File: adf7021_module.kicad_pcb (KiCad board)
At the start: 4 copper layers, 62.5 x 28 mm, 75 parts, among them J1 Conn_Board2Board, J2 Conn_Coaxial, J3 Conn_Coaxial, J4 Conn_goldpin, J5 Conn_Coaxial, J6 Conn_Coaxial, J7 RFShield_OnePiece, U1 ADF7021, X1 19.68MHz

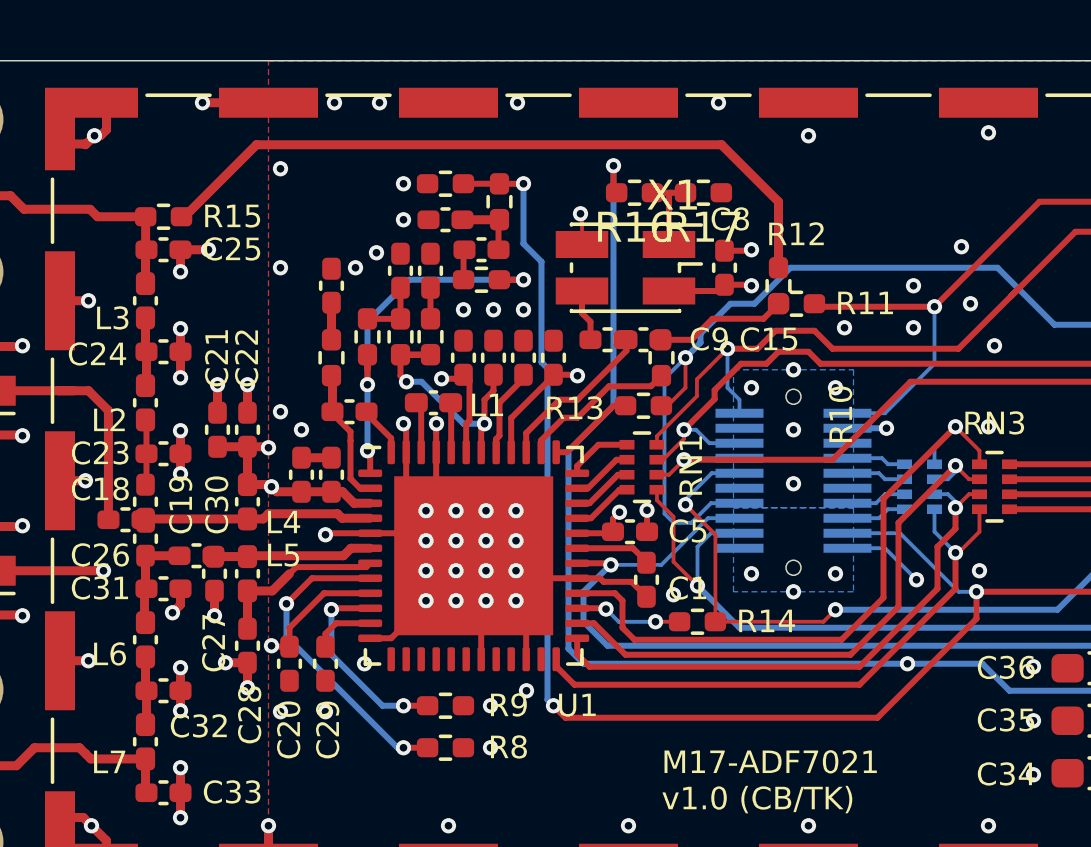
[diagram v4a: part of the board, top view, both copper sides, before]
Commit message: adding fab outputs
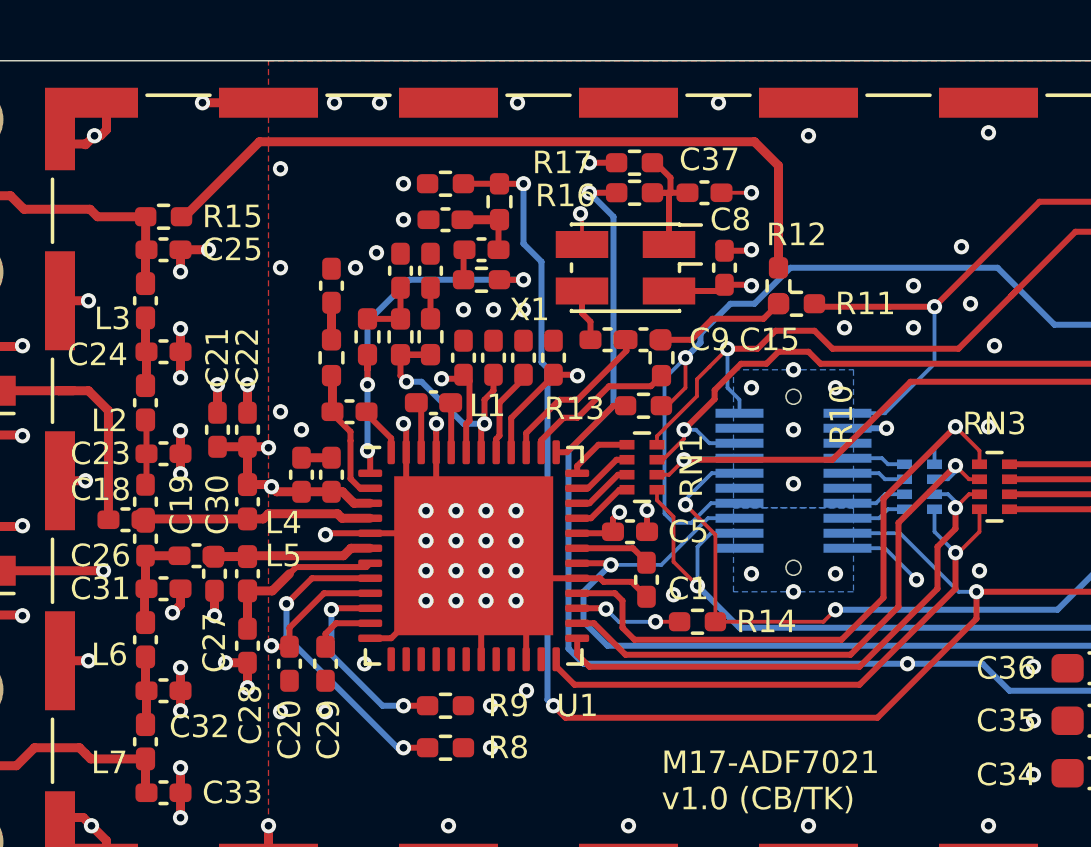
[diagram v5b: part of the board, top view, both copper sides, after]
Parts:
- added C37: 10n, Capacitor_SMD:C_0402_1005Metric_Pad0.74x0.62mm_HandSolder, F.Cu at (134.5, 47.4)
- R11: value 0 -> 0R
- R3: value 2 -> 2R
- X1: value 19.68MHz -> 12.288MHz
- moved R17 2.51 mm to (132.2, 46.4), turned to 0 degrees
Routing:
- net GND: track 73.5 -> 75.4 mm, vias 101 -> 103
- net Net-(C37-Pad1): track 2.85 -> 4.16 mm
- net CLK_SMA: track 23.9 -> 24.7 mm
- net VCO_MOD: track 57.2 -> 56.5 mm
